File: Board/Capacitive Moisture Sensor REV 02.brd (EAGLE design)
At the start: 165.1 x 63.5 mm, 20 parts, among them U1 TLC555CP, U2 LM358N, X1 22-23-2041

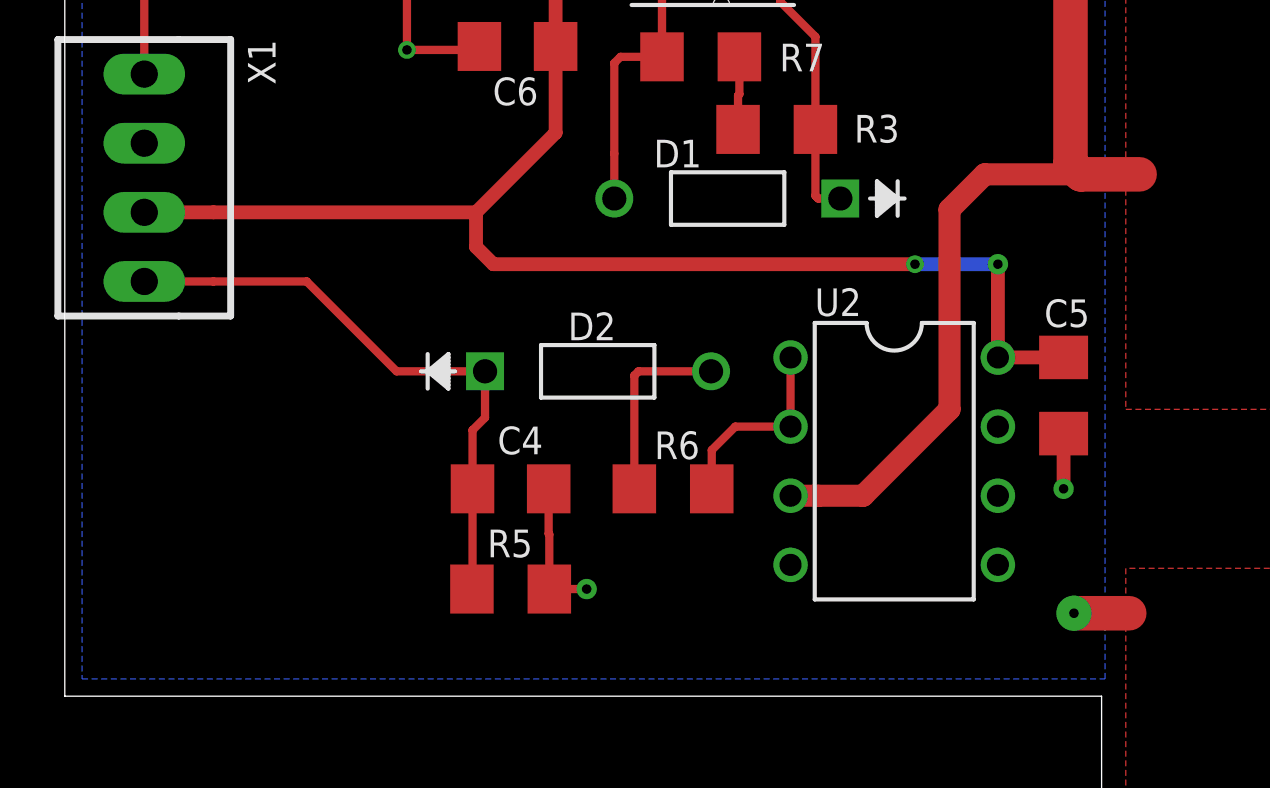
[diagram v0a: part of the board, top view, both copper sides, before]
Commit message: Completed board layout for rework modification
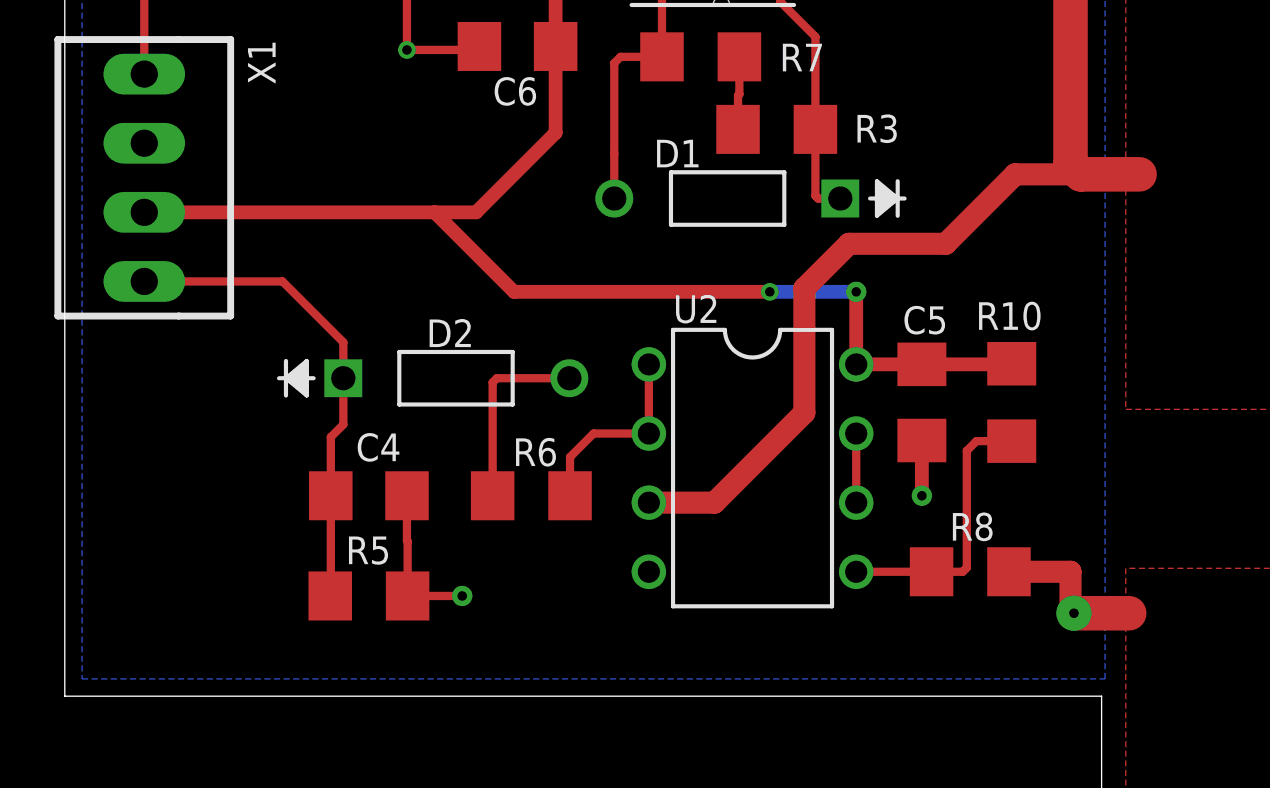
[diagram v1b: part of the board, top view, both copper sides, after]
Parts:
- added R10, R8: 1M, rcl:R1206
- C3: value 100pF -> 10nF
- R1: value 4.7k -> 3.3k
- R2: value 680 -> 3.3k
- R3: value 1k -> 10k
- R4: value 5.1k -> 750k
- R9: value 1k -> 3.3k
- moved C5 5.21 mm to (31.5, 10.8)
- moved R6 5.21 mm to (17.1, 7.37)
- moved U2 5.21 mm to (25.3, 8.38)
- moved C4 5.21 mm to (11.2, 7.37)
- moved R5 5.21 mm to (11.2, 3.68)
- moved D2 5.21 mm to (18.5, 11.7)
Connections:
- new net N$1: U2.6, U2.7
- new net N$11: R10.2, R8.1, U2.5
- net +5V: now also R10.1
- net GND: now also R8.2; no longer U2.5, U2.6, U2.7
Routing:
- net N$11: track 0.00 -> 10.2 mm
- net GND: track 28.0 -> 32.5 mm
- net OUTPUT: track 22.1 -> 17.8 mm
- net N$7: track 37.7 -> 41.4 mm
- net N$1: track 0.00 -> 2.54 mm
- net +5V: track 80.7 -> 79.3 mm

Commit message: Updated text in schematic
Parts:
- moved DRILEGEND 73.9 mm to (64.4, -26.3)
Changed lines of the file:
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@@
 <?xml version="1.0" encoding="utf-8"?>
 <!DOCTYPE eagle SYSTEM "eagle.dtd">
-<eagle version="9.6.1">
+<eagle version="9.6.2">
 <drawing>
 <settings>
@@
 <dimension x1="0" y1="38.1" x2="0" y2="0" x3="-6.35" y3="19.05" textsize="1.778" layer="47" unit="mil"/>
 <dimension x1="38.1" y1="50.8" x2="38.1" y2="38.1" x3="0.508" y3="44.45" textsize="1.778" layer="47" unit="mil"/>
-<text x="-28.15381875" y="-25.7835" size="1.778" layer="144">LAYER-STACK</text>
-<text x="-18.37481875" y="-28.7172" size="1.778" layer="145">01-16</text>
+<text x="45.76018125" y="-26.2915" size="1.778" layer="144">LAYER-STACK</text>
+<text x="55.53918125" y="-29.2252" size="1.778" layer="145">01-16</text>
 <wire x1="24.765" y1="30.861" x2="24.765" y2="29.845" width="0.1016" layer="145"/>
 <wire x1="24.257" y1="30.353" x2="25.273" y2="30.353" width="0.1016" layer="145"/>
@@
 <attribute name="POPULARITY" value="21" x="2.921" y="19.05" size="1.778" layer="27" rot="R270" display="off"/>
 </element>
-<element name="DRILEGEND" library="drilegend" package="DRILEGEND" value="" x="-9.48481875" y="-25.783490625" smashed="yes"/>
+<element name="DRILEGEND" library="drilegend" package="DRILEGEND" value="" x="64.42918125" y="-26.291490625" smashed="yes"/>
 <element name="R8" library="rcl" library_urn="urn:adsk.eagle:library:334" package="R1206" package3d_urn="urn:adsk.eagle:package:23540/2" value="1M" x="33.274" y="4.572" smashed="yes">
 <attribute name="NAME" x="32.512" y="5.715" size="1.016" layer="25" font="vector" ratio="17"/>
